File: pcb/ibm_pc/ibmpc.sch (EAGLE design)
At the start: 49 parts, among them IC1 STM32F072C8T6, SW1 324_SW, SW2 324_SW, U1 MAX3232

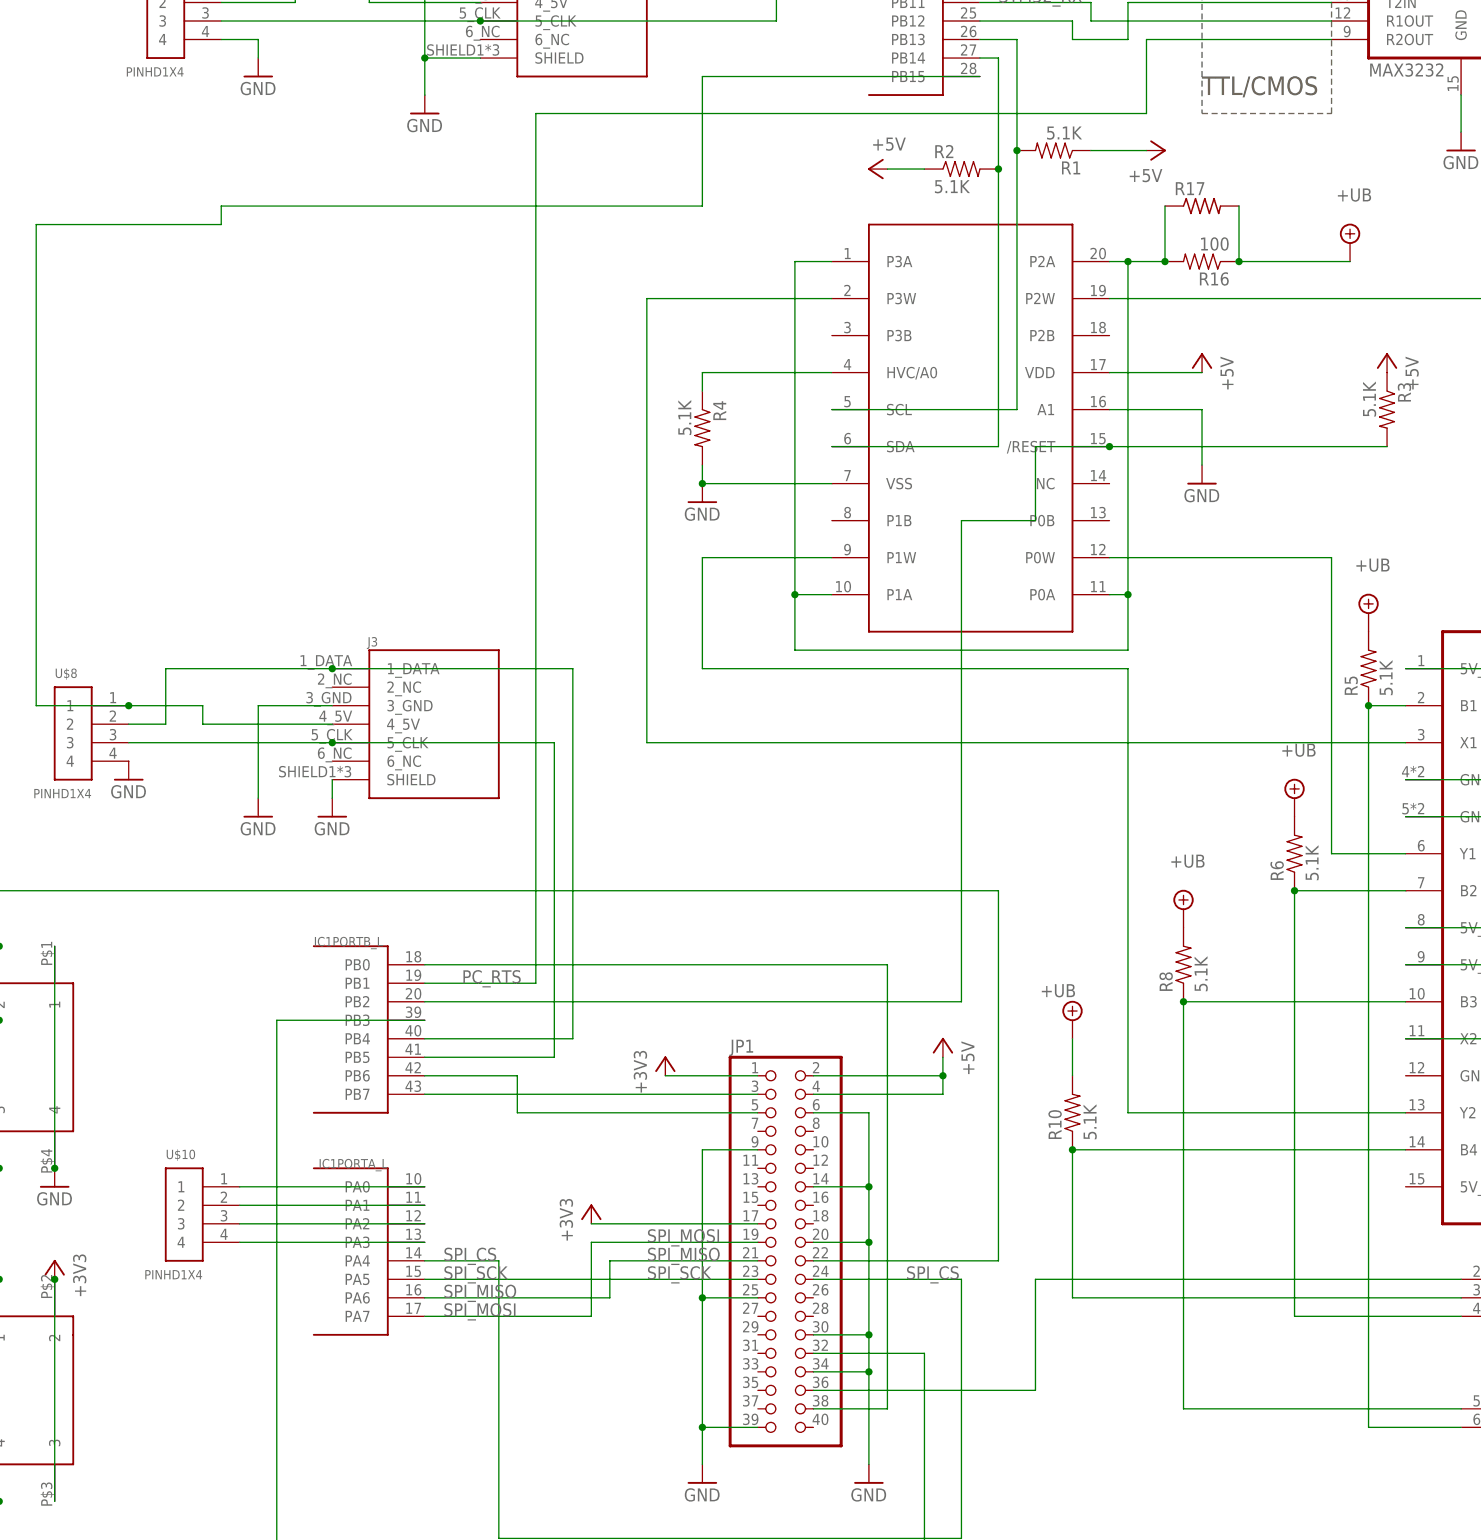
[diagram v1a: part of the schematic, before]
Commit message: updated IBM PC card
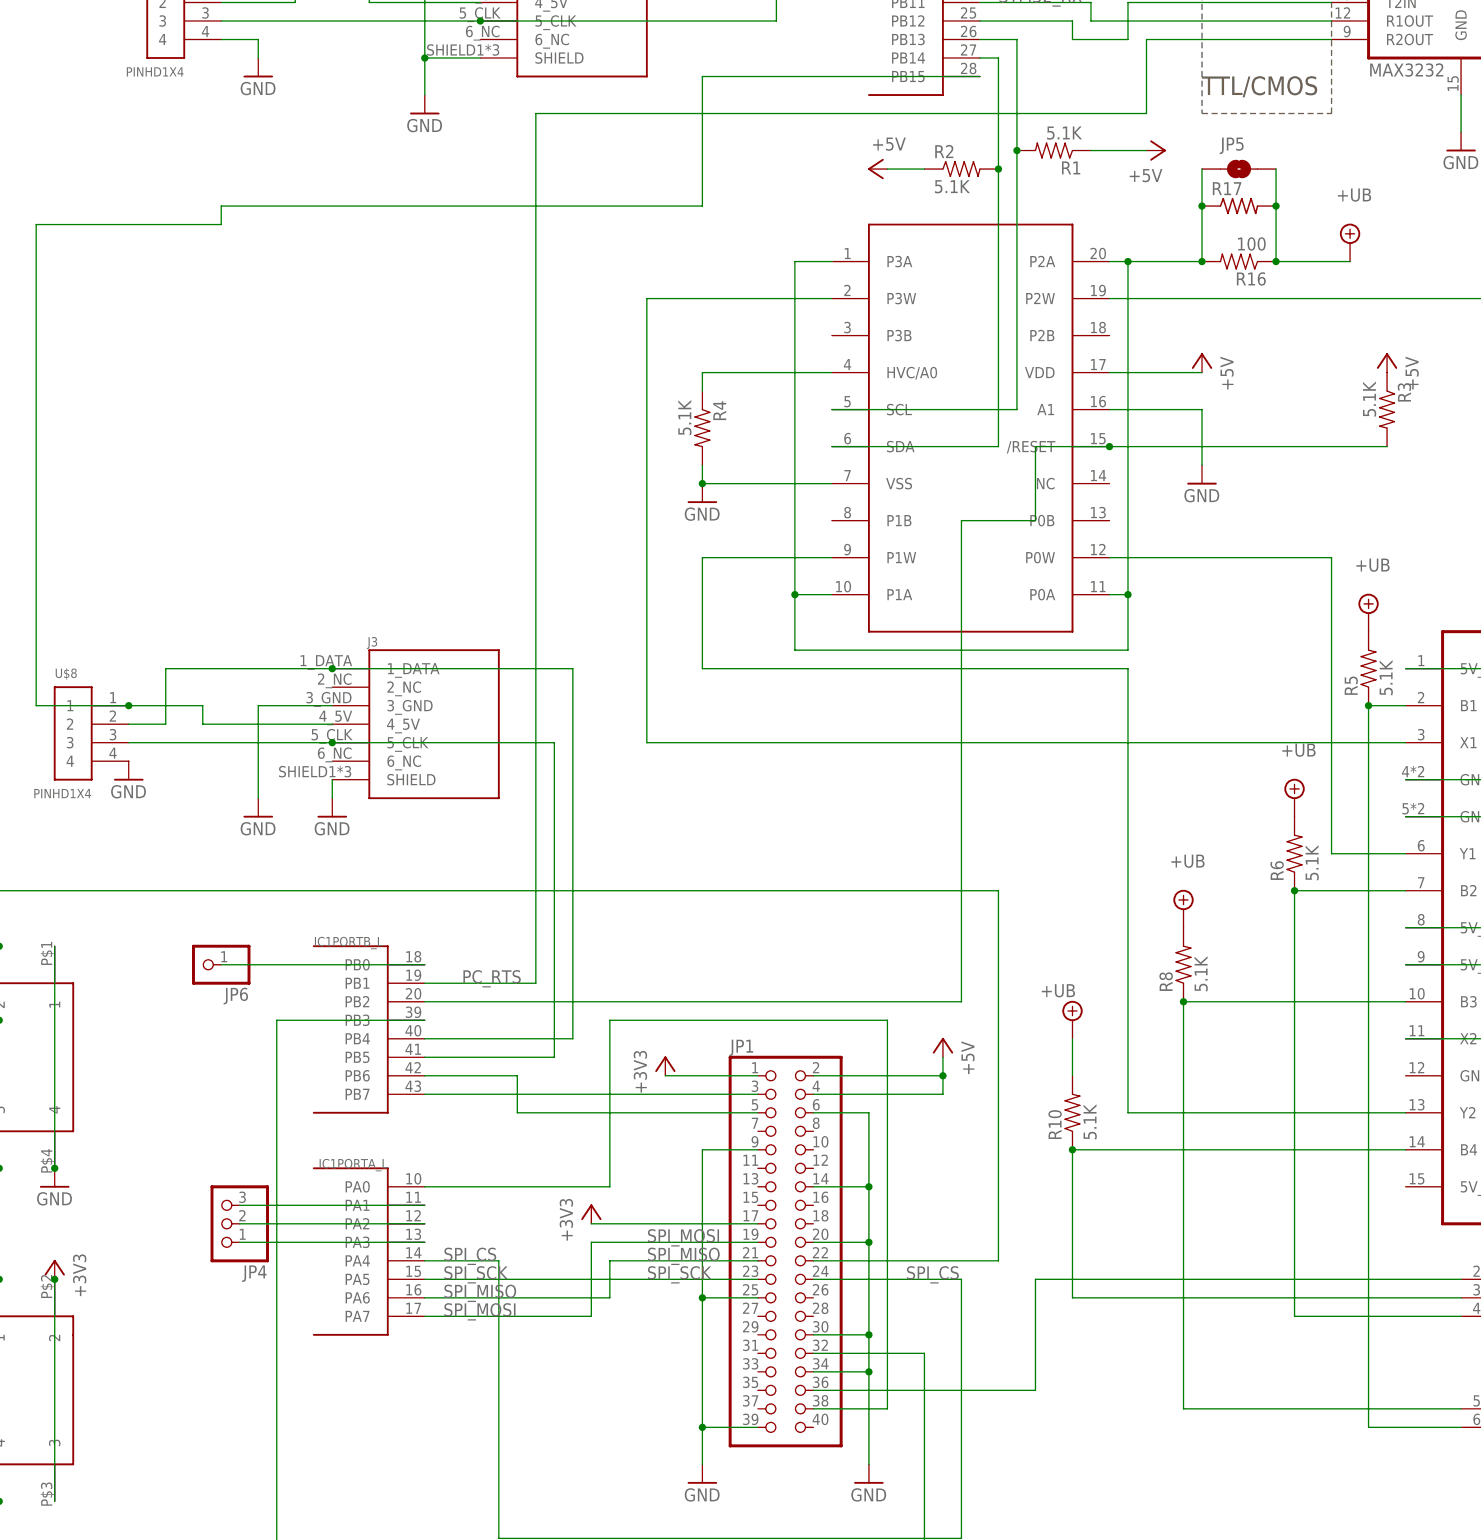
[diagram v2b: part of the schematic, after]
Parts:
- removed U$10: PINHD1X4, adafruit_changed:PINHD1X4
- added JP4: (no value), adafruit:PINHD-1X3CB
- added JP5: JUMPER-SMT_2_NO_NO-SILK, SparkFun-Jumpers:JUMPER-SMT_2_NO_NO-SILK
- added JP6: (no value), adafruit:PINHD-1X1CB
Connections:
- removed net N$38: IC1PORTA_L.PA0, U$10.1
- new net N$30: IC1PORTB_L.PB0, JP6.1
- net +UB: now also JP5.2
- net N$17: now also JP5.1
- net N$3: now also IC1PORTA_L.PA0; no longer IC1PORTB_L.PB0
- net N$39: now also JP4.3; no longer U$10.2
- net N$40: now also JP4.2; no longer U$10.3
- net N$41: now also JP4.1; no longer U$10.4
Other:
- moved on the sheet: R16, R17
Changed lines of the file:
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@@
 <part name="R4" library="SparkFun-Passives" deviceset="RESISTOR" device="0805-RES" value="5.1K"/>
 <part name="GND25" library="backplane" deviceset="GND" device=""/>
-<part name="U$10" library="adafruit_changed" deviceset="PINHD1X4" device=""/>
 <part name="R1" library="SparkFun-Passives" deviceset="RESISTOR" device="0805-RES" value="5.1K"/>
 <part name="R2" library="SparkFun-Passives" deviceset="RESISTOR" device="0805-RES" value="5.1K"/>
@@
 <part name="R16" library="SparkFun-Passives" deviceset="RESISTOR" device="0805-RES" value="100"/>
 <part name="R17" library="adafruit" deviceset="R-US_" device="0204/7"/>
+<part name="JP4" library="adafruit" deviceset="PINHD-1X3" device="CB"/>
+<part name="JP5" library="SparkFun-Jumpers" deviceset="JUMPER-SMT_2_NO" device="_NO-SILK"/>
+<part name="JP6" library="adafruit" deviceset="PINHD-1X1" device="CB"/>
 </parts>
 <sheets>
@@
 <attribute name="VALUE" x="17.78" y="76.2" size="1.778" layer="96"/>
 </instance>
-<instance part="U$10" gate="1" x="12.7" y="25.4" smashed="yes" rot="MR0">
-<attribute name="NAME" x="7.62" y="33.02" size="1.27" layer="95" font="vector" rot="MR180"/>
-<attribute name="VALUE" x="12.7" y="15.24" size="1.27" layer="96" font="vector" rot="MR0"/>
-</instance>
 <instance part="R1" gate="G$1" x="129.54" y="170.18" smashed="yes" rot="R180">
 <attribute name="NAME" x="133.35" y="168.6814" size="1.778" layer="95" rot="R180"/>
@@
 <attribute name="VALUE" x="168.275" y="163.195" size="1.778" layer="96"/>
 </instance>
-<instance part="R16" gate="G$1" x="149.86" y="154.94" smashed="yes" rot="R180">
-<attribute name="NAME" x="153.67" y="153.4414" size="1.778" layer="95" rot="R180"/>
-<attribute name="VALUE" x="153.67" y="158.242" size="1.778" layer="96" rot="R180"/>
-</instance>
-<instance part="R17" gate="G$1" x="149.86" y="162.56" smashed="yes">
-<attribute name="NAME" x="146.05" y="164.0586" size="1.778" layer="95"/>
-<attribute name="VALUE" x="146.05" y="159.258" size="1.778" layer="96"/>
+<instance part="R16" gate="G$1" x="154.94" y="154.94" smashed="yes" rot="R180">
+<attribute name="NAME" x="158.75" y="153.4414" size="1.778" layer="95" rot="R180"/>
+<attribute name="VALUE" x="158.75" y="158.242" size="1.778" layer="96" rot="R180"/>
+</instance>
+<instance part="R17" gate="G$1" x="154.94" y="162.56" smashed="yes">
+<attribute name="NAME" x="151.13" y="164.0586" size="1.778" layer="95"/>
+<attribute name="VALUE" x="151.13" y="159.258" size="1.778" layer="96"/>
+</instance>
+<instance part="JP4" gate="A" x="15.24" y="22.86" smashed="yes" rot="R180">
+<attribute name="NAME" x="21.59" y="17.145" size="1.778" layer="95" rot="R180"/>
+<attribute name="VALUE" x="21.59" y="30.48" size="1.778" layer="96" rot="R180"/>
+</instance>
+<instance part="JP5" gate="G$1" x="154.94" y="167.64" smashed="yes">
+<attribute name="NAME" x="152.4" y="170.18" size="1.778" layer="95" font="vector"/>
+</instance>
+<instance part="JP6" gate="G$1" x="12.7" y="58.42" smashed="yes" rot="R180">
+<attribute name="NAME" x="19.05" y="55.245" size="1.778" layer="95" rot="R180"/>
+<attribute name="VALUE" x="19.05" y="63.5" size="1.778" layer="96" rot="R180"/>
 </instance>
 </instances>
@@
 <pinref part="R16" gate="G$1" pin="1"/>
 <pinref part="SUPPLY6" gate="G$1" pin="+UB"/>
-<wire x1="154.94" y1="154.94" x2="170.18" y2="154.94" width="0.1524" layer="91"/>
+<wire x1="160.02" y1="154.94" x2="170.18" y2="154.94" width="0.1524" layer="91"/>
 <pinref part="R17" gate="G$1" pin="2"/>
-<wire x1="154.94" y1="162.56" x2="154.94" y2="154.94" width="0.1524" layer="91"/>
-<junction x="154.94" y="154.94"/>
+<wire x1="160.02" y1="162.56" x2="160.02" y2="154.94" width="0.1524" layer="91"/>
+<junction x="160.02" y="154.94"/>
+<pinref part="JP5" gate="G$1" pin="2"/>
+<wire x1="160.02" y1="167.64" x2="160.02" y2="162.56" width="0.1524" layer="91"/>
+<junction x="160.02" y="162.56"/>
 </segment>
 </net>
@@
 </segment>
 </net>
-<net name="N$38" class="0">
-<segment>
-<pinref part="IC1" gate="PORTA_L" pin="PA0"/>
-<pinref part="U$10" gate="1" pin="1"/>
-<wire x1="43.18" y1="27.94" x2="17.78" y2="27.94" width="0.1524" layer="91"/>
-</segment>
-</net>
 <net name="N$39" class="0">
 <segment>
 <pinref part="IC1" gate="PORTA_L" pin="PA1"/>
-<pinref part="U$10" gate="1" pin="2"/>
 <wire x1="43.18" y1="25.4" x2="17.78" y2="25.4" width="0.1524" layer="91"/>
+<pinref part="JP4" gate="A" pin="3"/>
 </segment>
 </net>
@@
 <segment>
 <pinref part="IC1" gate="PORTA_L" pin="PA2"/>
-<pinref part="U$10" gate="1" pin="3"/>
 <wire x1="43.18" y1="22.86" x2="17.78" y2="22.86" width="0.1524" layer="91"/>
+<pinref part="JP4" gate="A" pin="2"/>
 </segment>
 </net>
@@
 <segment>
 <pinref part="IC1" gate="PORTA_L" pin="PA3"/>
-<pinref part="U$10" gate="1" pin="4"/>
 <wire x1="43.18" y1="20.32" x2="17.78" y2="20.32" width="0.1524" layer="91"/>
+<pinref part="JP4" gate="A" pin="1"/>
 </segment>
 </net>
@@
 <net name="N$3" class="0">
 <segment>
-<pinref part="IC1" gate="PORTB_L" pin="PB0"/>
-<wire x1="43.18" y1="58.42" x2="106.68" y2="58.42" width="0.1524" layer="91"/>
-<wire x1="106.68" y1="58.42" x2="106.68" y2="-2.54" width="0.1524" layer="91"/>
 <pinref part="JP1" gate="A" pin="38"/>
+<wire x1="106.68" y1="50.8" x2="106.68" y2="-2.54" width="0.1524" layer="91"/>
 <wire x1="106.68" y1="-2.54" x2="96.52" y2="-2.54" width="0.1524" layer="91"/>
+<pinref part="IC1" gate="PORTA_L" pin="PA0"/>
+<wire x1="43.18" y1="27.94" x2="68.58" y2="27.94" width="0.1524" layer="91"/>
+<wire x1="68.58" y1="27.94" x2="68.58" y2="50.8" width="0.1524" layer="91"/>
+<wire x1="68.58" y1="50.8" x2="106.68" y2="50.8" width="0.1524" layer="91"/>
 </segment>
 </net>
@@
 <junction x="139.7" y="154.94"/>
 <pinref part="R16" gate="G$1" pin="2"/>
-<wire x1="139.7" y1="154.94" x2="144.78" y2="154.94" width="0.1524" layer="91"/>
+<wire x1="139.7" y1="154.94" x2="149.86" y2="154.94" width="0.1524" layer="91"/>
 <pinref part="R17" gate="G$1" pin="1"/>
-<wire x1="144.78" y1="162.56" x2="144.78" y2="154.94" width="0.1524" layer="91"/>
-<junction x="144.78" y="154.94"/>
-</segment>
-</net>
+<wire x1="149.86" y1="162.56" x2="149.86" y2="154.94" width="0.1524" layer="91"/>
+<junction x="149.86" y="154.94"/>
+<pinref part="JP5" gate="G$1" pin="1"/>
+<wire x1="149.86" y1="167.64" x2="149.86" y2="162.56" width="0.1524" layer="91"/>
+<junction x="149.86" y="162.56"/>
+</segment>
+</net>
+<net name="N$30" class="0">
+<segment>
+<pinref part="IC1" gate="PORTB_L" pin="PB0"/>
+<pinref part="JP6" gate="G$1" pin="1"/>
+<wire x1="43.18" y1="58.42" x2="15.24" y2="58.42" width="0.1524" layer="91"/>
+</segment>
+</net>
